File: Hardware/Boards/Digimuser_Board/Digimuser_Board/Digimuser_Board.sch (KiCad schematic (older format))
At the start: 59 parts, among them J1 Conn_01x01, J2 Conn_01x01, J4 Conn_01x03, U1 MCP6272

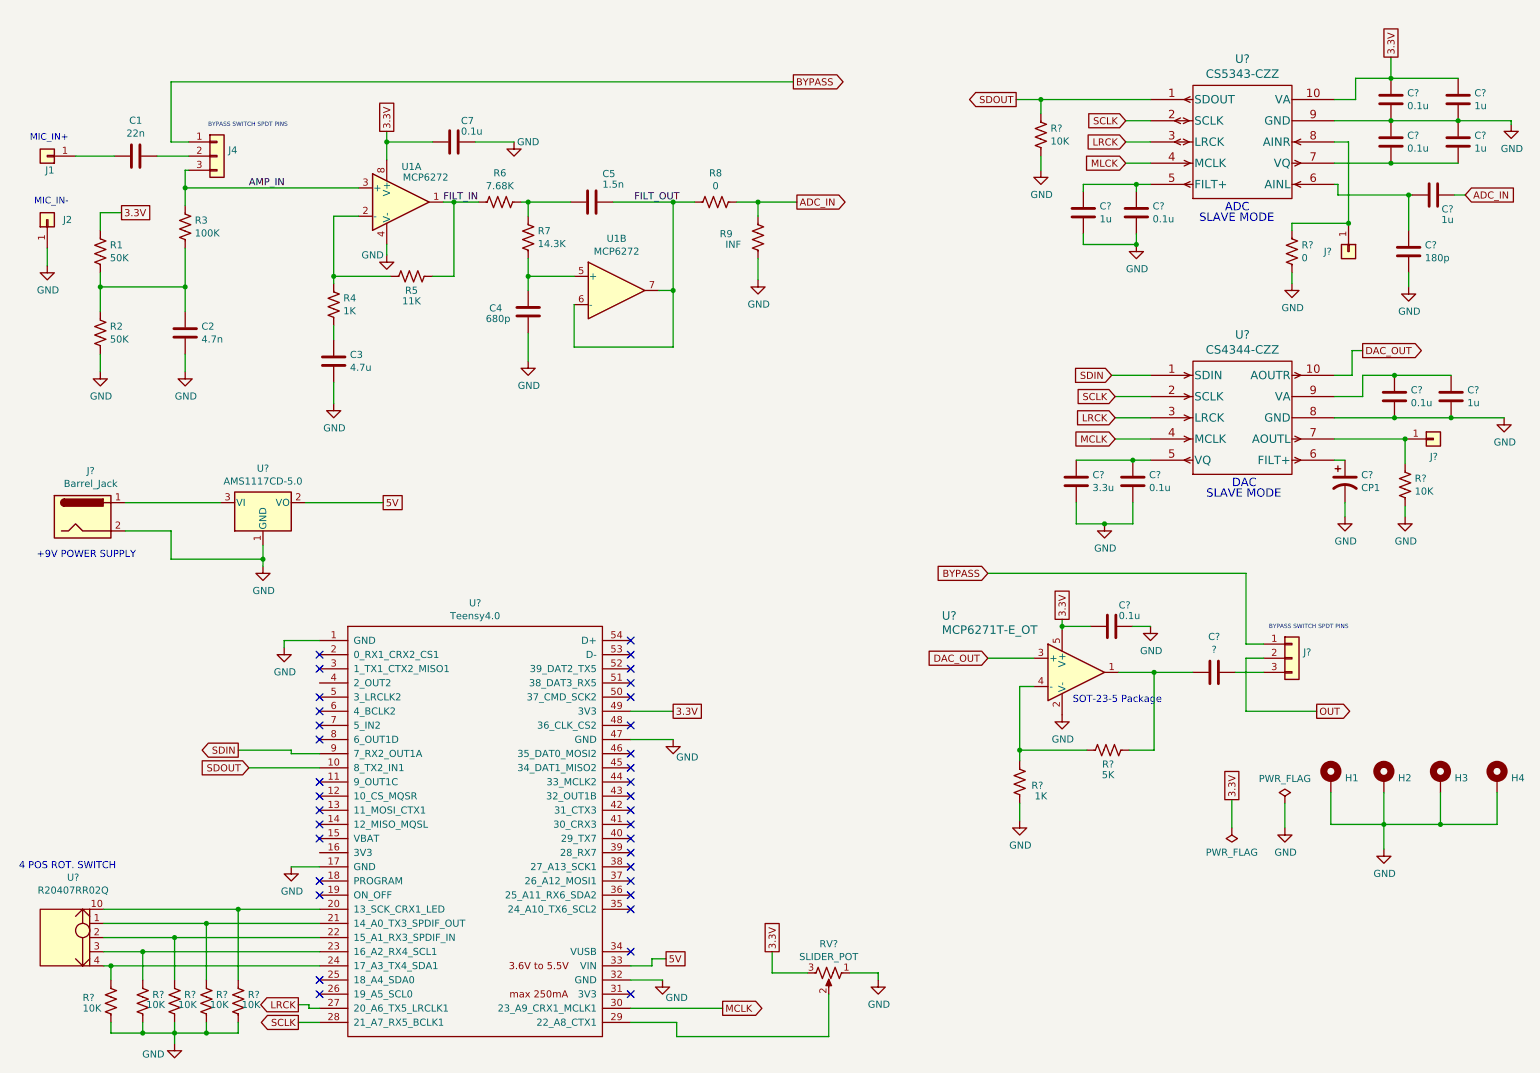
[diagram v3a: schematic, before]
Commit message: Assigned PCB footprints to all the components. Some components may need footprints revised.
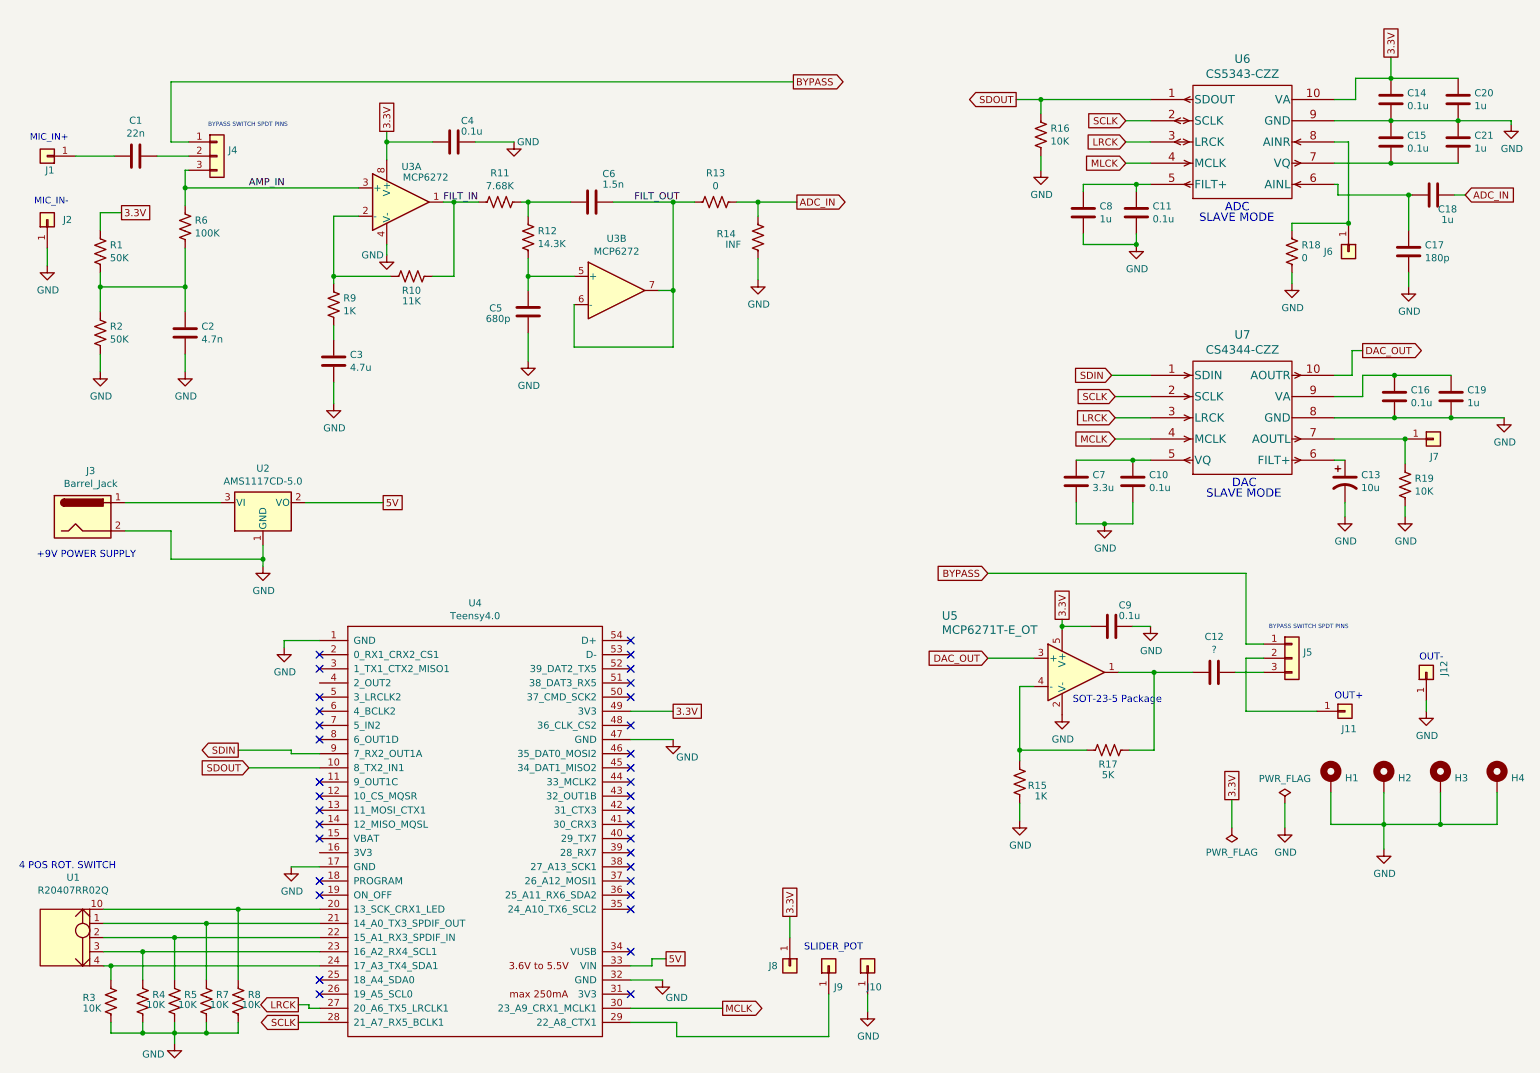
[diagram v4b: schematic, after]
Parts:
- removed RV?: SLIDER_POT, symbol Device:R_POT_US
- added J10, J11, J12, J8, J9: Conn_01x01, Connector_Pin:Pin_D1.3mm_L11.0mm_LooseFit, symbol Connector_Generic:Conn_01x01
- C1, C2, C3: footprint Capacitor_THT:C_Disc_D7.5mm_W4.4mm_P5.00mm -> Capacitor_SMD:C_0805_2012Metric
- C10, C11, C12, C14, C15, C16, C17, C18, C19, C20, C21, C7, C8, C9: renamed from C?; footprint Capacitor_THT:C_Disc_D7.5mm_W4.4mm_P5.00mm -> Capacitor_SMD:C_0805_2012Metric
- C13: renamed from C?; value CP1 -> 10u; footprint (none) -> Capacitor_THT:CP_Radial_D6.3mm_P2.50mm
- C4: renamed from C7; footprint Capacitor_THT:C_Disc_D7.5mm_W4.4mm_P5.00mm -> Capacitor_SMD:C_0805_2012Metric
- C5: renamed from C4; footprint Capacitor_THT:C_Disc_D7.5mm_W4.4mm_P5.00mm -> Capacitor_SMD:C_0805_2012Metric
- C6: renamed from C5; footprint Capacitor_THT:C_Disc_D7.5mm_W4.4mm_P5.00mm -> Capacitor_SMD:C_0805_2012Metric
- J3: renamed from J?; footprint (none) -> Connector_BarrelJack:BarrelJack_Horizontal
- J4: footprint Connector_PinSocket_2.54mm:PinSocket_1x03_P2.54mm_Vertical -> Connector_PinHeader_2.54mm:PinHeader_1x03_P2.54mm_Vertical
- J5: renamed from J?; footprint Connector_PinSocket_2.54mm:PinSocket_1x03_P2.54mm_Vertical -> Connector_PinHeader_2.54mm:PinHeader_1x03_P2.54mm_Vertical
- J6, J7: renamed from J?; footprint Connector_PinSocket_2.54mm:PinSocket_1x01_P2.54mm_Vertical -> Connector_Pin:Pin_D1.3mm_L11.0mm_LooseFit
- R1, R2: footprint Resistor_THT:R_Axial_DIN0207_L6.3mm_D2.5mm_P10.16mm_Horizontal -> Resistor_SMD:R_0805_2012Metric
- R10: renamed from R5; footprint Resistor_THT:R_Axial_DIN0207_L6.3mm_D2.5mm_P10.16mm_Horizontal -> Resistor_SMD:R_0805_2012Metric
- R11: renamed from R6; footprint Resistor_THT:R_Axial_DIN0207_L6.3mm_D2.5mm_P10.16mm_Horizontal -> Resistor_SMD:R_0805_2012Metric
- R12: renamed from R7; footprint Resistor_THT:R_Axial_DIN0207_L6.3mm_D2.5mm_P10.16mm_Horizontal -> Resistor_SMD:R_0805_2012Metric
- R13: renamed from R8; footprint Resistor_THT:R_Axial_DIN0207_L6.3mm_D2.5mm_P10.16mm_Horizontal -> Resistor_SMD:R_0805_2012Metric
- R14: renamed from R9; footprint Resistor_THT:R_Axial_DIN0207_L6.3mm_D2.5mm_P10.16mm_Horizontal -> Resistor_SMD:R_0805_2012Metric
- R15, R16, R17, R18, R19, R3, R4, R5, R7, R8: renamed from R?; footprint Resistor_THT:R_Axial_DIN0207_L6.3mm_D2.5mm_P10.16mm_Horizontal -> Resistor_SMD:R_0805_2012Metric
- R6: renamed from R3; footprint Resistor_THT:R_Axial_DIN0207_L6.3mm_D2.5mm_P10.16mm_Horizontal -> Resistor_SMD:R_0805_2012Metric
- R9: renamed from R4; footprint Resistor_THT:R_Axial_DIN0207_L6.3mm_D2.5mm_P10.16mm_Horizontal -> Resistor_SMD:R_0805_2012Metric
- U1: renamed from U?; footprint (none) -> Connector_PinSocket_2.54mm:PinSocket_1x04_P2.54mm_Vertical
- U3: renamed from U1; footprint Package_DIP:DIP-8_W7.62mm -> MCP6272-E_SN:SOIC127P600X175-8N
- U4: renamed from U?; footprint (none) -> teensy:Teensy40
- U5: renamed from U?; footprint SOT-23-5_MC_MCH -> MCP6271TE0T:MCP6271T-E&slash_OT
- U6: renamed from U?; footprint CIR-TSSOP-10 -> CS5343CZZ:CS5343-CZZ
- U7: renamed from U?; footprint CIR-TSSOP-10 -> CS4344CZZ:CS4344-CZZ
- gave numbers to parts that had none: 1
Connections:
- net 3.3V: now also J8.1 (Pin_1)
- net GND: now also J10.1 (Pin_1), J12.1 (Pin_1)
- net at U4.29 (22_A8_CTX1): now also J9.1 (Pin_1)
- net OUT: no longer names the net of J5.2 (Pin_2)
- net OUT: now also J11.1 (Pin_1)
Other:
- note added: "OUT+"
- note added: "OUT-"
- note added: "SLIDER_POT"

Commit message: Started the PCB layout. Also had to find a new voltage regulator.
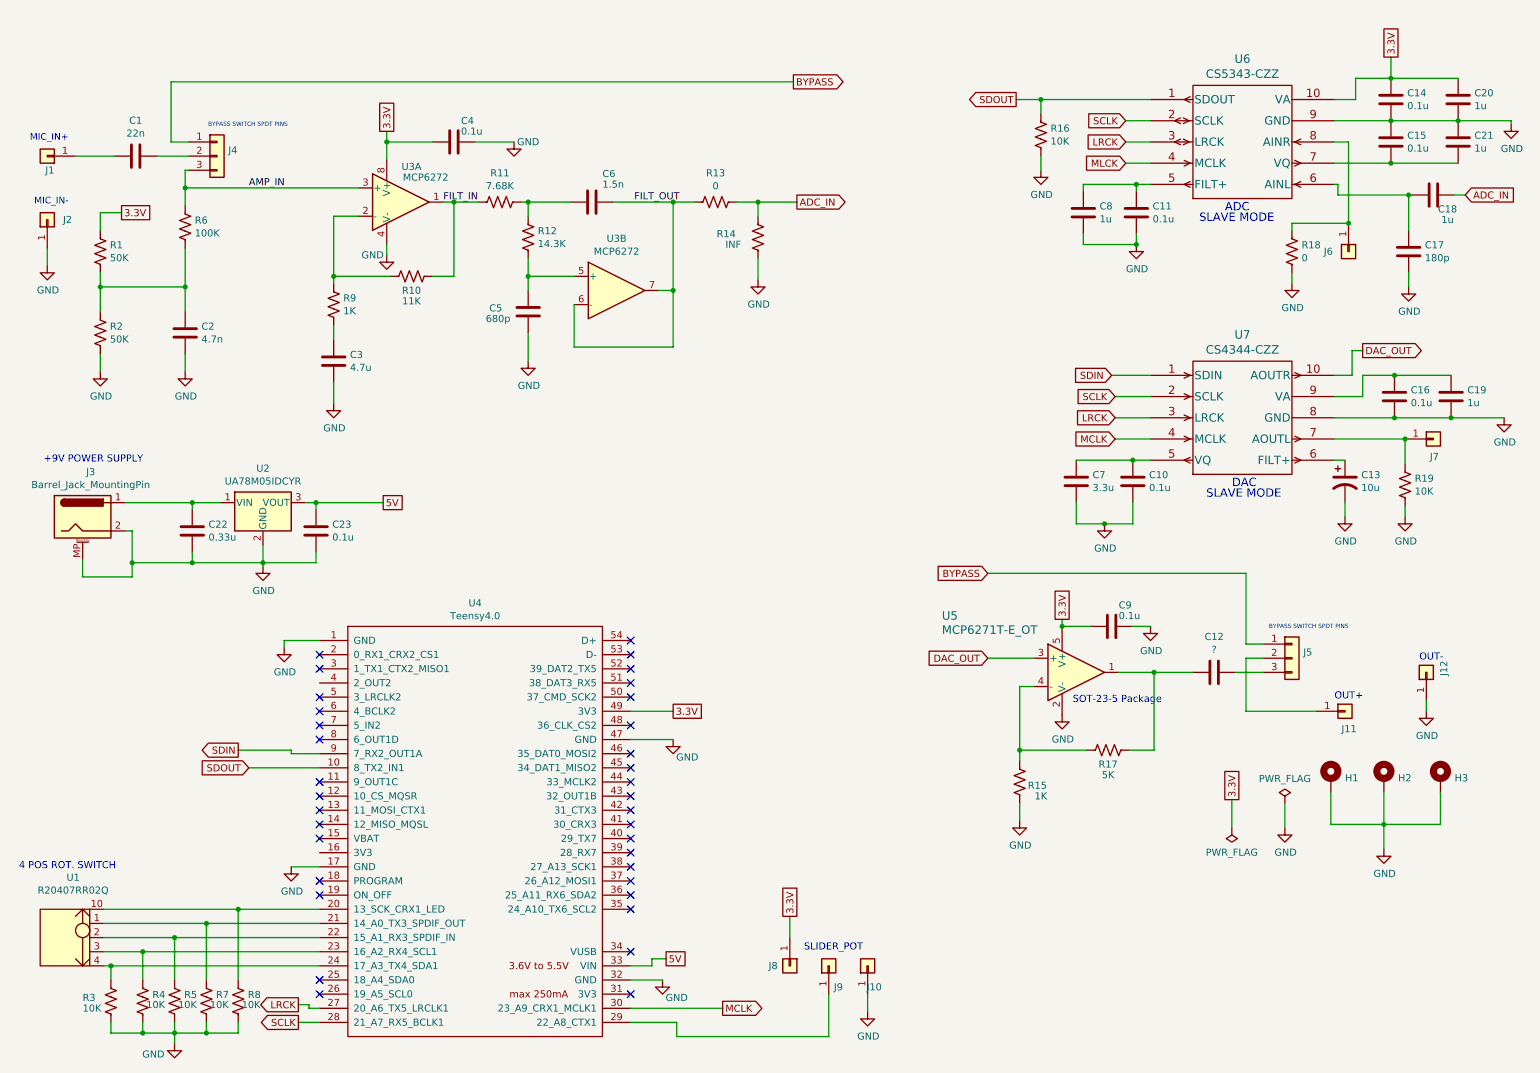
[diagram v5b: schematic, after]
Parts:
- removed H4: MountingHole_Pad, MountingHole:MountingHole_3.2mm_M3_Pad, symbol Mechanical:MountingHole_Pad
- removed J3: Barrel_Jack, Connector_BarrelJack:BarrelJack_Horizontal, symbol Connector:Barrel_Jack
- removed U2: AMS1117CD-5.0, Package_TO_SOT_SMD:TO-252-3_TabPin2, symbol Regulator_Linear:AMS1117CD-5.0
- added C22: 0.33u, Capacitor_SMD:C_0805_2012Metric, symbol Device:C
- added C23: 0.1u, Capacitor_SMD:C_0805_2012Metric, symbol Device:C
- added J3: Barrel_Jack_MountingPin, Connector_BarrelJack:BarrelJack_Horizontal, symbol Connector:Barrel_Jack_MountingPin
- added U2: UA78M05IDCYR, Package_TO_SOT_SMD:SOT-223, symbol Regulator_Linear:AP2204R-5.0
- H1, H2, H3: footprint MountingHole:MountingHole_3.2mm_M3_Pad -> MountingHole:MountingHole_2.2mm_M2_Pad
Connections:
- net 5V: now also C23.1, U2.3 (VOUT)
- net GND: now also C22.2, C23.2, J3.2, J3.MP (MountPin), U2.2 (GND)
- new net: C22.1, J3.1, U2.1 (VIN)
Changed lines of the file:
@@
 F 0 "H1" H 9925 5803 50  0000 L CNN
 F 1 "MountingHole_Pad" H 9925 5758 50  0001 L CNN
-F 2 "MountingHole:MountingHole_3.2mm_M3_Pad" H 9825 5800 50  0001 C CNN
+F 2 "MountingHole:MountingHole_2.2mm_M2_Pad" H 9825 5800 50  0001 C CNN
 F 3 "~" H 9825 5800 50  0001 C CNN
 	1    9825 5800
@@
 F 0 "H2" H 10300 5803 50  0000 L CNN
 F 1 "MountingHole_Pad" H 10300 5758 50  0001 L CNN
-F 2 "MountingHole:MountingHole_3.2mm_M3_Pad" H 10200 5800 50  0001 C CNN
+F 2 "MountingHole:MountingHole_2.2mm_M2_Pad" H 10200 5800 50  0001 C CNN
 F 3 "~" H 10200 5800 50  0001 C CNN
 	1    10200 5800
@@
 F 0 "H3" H 10700 5803 50  0000 L CNN
 F 1 "MountingHole_Pad" H 10700 5758 50  0001 L CNN
-F 2 "MountingHole:MountingHole_3.2mm_M3_Pad" H 10600 5800 50  0001 C CNN
+F 2 "MountingHole:MountingHole_2.2mm_M2_Pad" H 10600 5800 50  0001 C CNN
 F 3 "~" H 10600 5800 50  0001 C CNN
 	1    10600 5800
 	1    0    0    -1
 $EndComp
-$Comp
-L Mechanical:MountingHole_Pad H4
-U 1 1 5F9CF59E
-P 11000 5800
-F 0 "H4" H 11100 5803 50  0000 L CNN
-F 1 "MountingHole_Pad" H 11100 5758 50  0001 L CNN
-F 2 "MountingHole:MountingHole_3.2mm_M3_Pad" H 11000 5800 50  0001 C CNN
-F 3 "~" H 11000 5800 50  0001 C CNN
-	1    11000 5800
-	1    0    0    -1
-$EndComp
 Wire Wire Line
 	9825 5900 9825 6125
@@
 	9825 6125 10200 6125
 Wire Wire Line
-	11000 6125 11000 5900
-Wire Wire Line
 	10600 5900 10600 6125
-Connection ~ 10600 6125
-Wire Wire Line
-	10600 6125 11000 6125
 Wire Wire Line
 	10200 5900 10200 6125
@@
 NoConn ~ 4875 6725
 NoConn ~ 4875 7025
-$Comp
-L Regulator_Linear:AMS1117CD-5.0 U2
-U 1 1 5FD128B2
-P 2275 3850
-F 0 "U2" H 2275 4092 50  0000 C CNN
-F 1 "AMS1117CD-5.0" H 2275 4001 50  0000 C CNN
-F 2 "Package_TO_SOT_SMD:TO-252-3_TabPin2" H 2275 4050 50  0001 C CNN
-F 3 "http://www.advanced-monolithic.com/pdf/ds1117.pdf" H 2375 3600 50  0001 C CNN
-	1    2275 3850
-	1    0    0    -1
-$EndComp
-$Comp
-L Connector:Barrel_Jack J3
-U 1 1 5FD23849
-P 1000 3950
-F 0 "J3" H 1057 4275 50  0000 C CNN
-F 1 "Barrel_Jack" H 1057 4184 50  0000 C CNN
-F 2 "Connector_BarrelJack:BarrelJack_Horizontal" H 1050 3910 50  0001 C CNN
-F 3 "~" H 1050 3910 50  0001 C CNN
-	1    1000 3950
-	1    0    0    -1
-$EndComp
-Wire Wire Line
-	1300 3850 1975 3850
-Wire Wire Line
-	1300 4050 1625 4050
-Wire Wire Line
-	1625 4050 1625 4250
-Wire Wire Line
-	1625 4250 2275 4250
-Wire Wire Line
-	2275 4250 2275 4150
+Wire Wire Line
+	1300 3850 1775 3850
+Wire Wire Line
+	1300 4050 1350 4050
 $Comp
 L power:GND #PWR05
@@
 	1    0    0    -1
 $EndComp
-Wire Wire Line
-	2275 4300 2275 4250
-Connection ~ 2275 4250
-Text Notes 675  4250 0    50   ~ 0
+Text Notes 725  3575 0    50   ~ 0
 +9V POWER SUPPLY
 Wire Wire Line
-	2575 3850 3125 3850
+	2575 3850 2650 3850
 Text GLabel 3125 3850 2    50   UnSpc ~ 0
 5V
@@
 Text Notes 6100 7025 0    50   ~ 0
 SLIDER_POT
+$Comp
+L Connector:Barrel_Jack_MountingPin J3
+U 1 1 5FC5DD80
+P 1000 3950
+F 0 "J3" H 1057 4267 50  0000 C CNN
+F 1 "Barrel_Jack_MountingPin" H 1057 4176 50  0000 C CNN
+F 2 "Connector_BarrelJack:BarrelJack_Horizontal" H 1050 3910 50  0001 C CNN
+F 3 "~" H 1050 3910 50  0001 C CNN
+	1    1000 3950
+	1    0    0    -1
+$EndComp
+Wire Wire Line
+	1000 4250 1000 4375
+Wire Wire Line
+	1000 4375 1350 4375
+Wire Wire Line
+	1350 4375 1350 4275
+Wire Wire Line
+	2275 4150 2275 4275
+$Comp
+L Device:C C22
+U 1 1 5FC79B88
+P 1775 4050
+F 0 "C22" H 1890 4096 50  0000 L CNN
+F 1 "0.33u" H 1890 4005 50  0000 L CNN
+F 2 "Capacitor_SMD:C_0805_2012Metric" H 1813 3900 50  0001 C CNN
+F 3 "~" H 1775 4050 50  0001 C CNN
+	1    1775 4050
+	1    0    0    -1
+$EndComp
+Wire Wire Line
+	1775 3900 1775 3850
+Connection ~ 1775 3850
+Wire Wire Line
+	1775 3850 1975 3850
+Wire Wire Line
+	1775 4200 1775 4275
+Wire Wire Line
+	1775 4275 2275 4275
+Connection ~ 2275 4275
+Wire Wire Line
+	2275 4275 2275 4300
+Wire Wire Line
+	1775 4275 1350 4275
+Connection ~ 1775 4275
+Connection ~ 1350 4275
+Wire Wire Line
+	1350 4275 1350 4050
+$Comp
+L Device:C C23
+U 1 1 5FCA4CF6
+P 2650 4050
+F 0 "C23" H 2765 4096 50  0000 L CNN
+F 1 "0.1u" H 2765 4005 50  0000 L CNN
+F 2 "Capacitor_SMD:C_0805_2012Metric" H 2688 3900 50  0001 C CNN
+F 3 "~" H 2650 4050 50  0001 C CNN
+	1    2650 4050
+	1    0    0    -1
+$EndComp
+Wire Wire Line
+	2650 3900 2650 3850
+Connection ~ 2650 3850
+Wire Wire Line
+	2650 3850 3125 3850
+Wire Wire Line
+	2650 4200 2650 4275
+Wire Wire Line
+	2650 4275 2275 4275
+$Comp
+L Regulator_Linear:AP2204R-5.0 U2
+U 1 1 5FCD2989
+P 2275 3850
+F 0 "U2" H 2275 4092 50  0000 C CNN
+F 1 "UA78M05IDCYR" H 2275 4001 50  0000 C CNN
+F 2 "Package_TO_SOT_SMD:SOT-223" H 2275 4075 50  0001 C CNN
+F 3 "https://www.diodes.com/assets/Datasheets/AP2204.pdf" H 2275 3850 50  0001 C CNN
+	1    2275 3850
+	1    0    0    -1
+$EndComp
 $EndSCHEMATC
